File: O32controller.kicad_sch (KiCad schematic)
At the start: 39 parts, among them J1 SWD Connector, J12 I2C/RS485_2, J2 BATT+, J3 BATT-, J7 BATT+, J8 BATT-, J9 I2C/RS485_1, U1 MA702GQ-P, U2 STSPIN32F0A

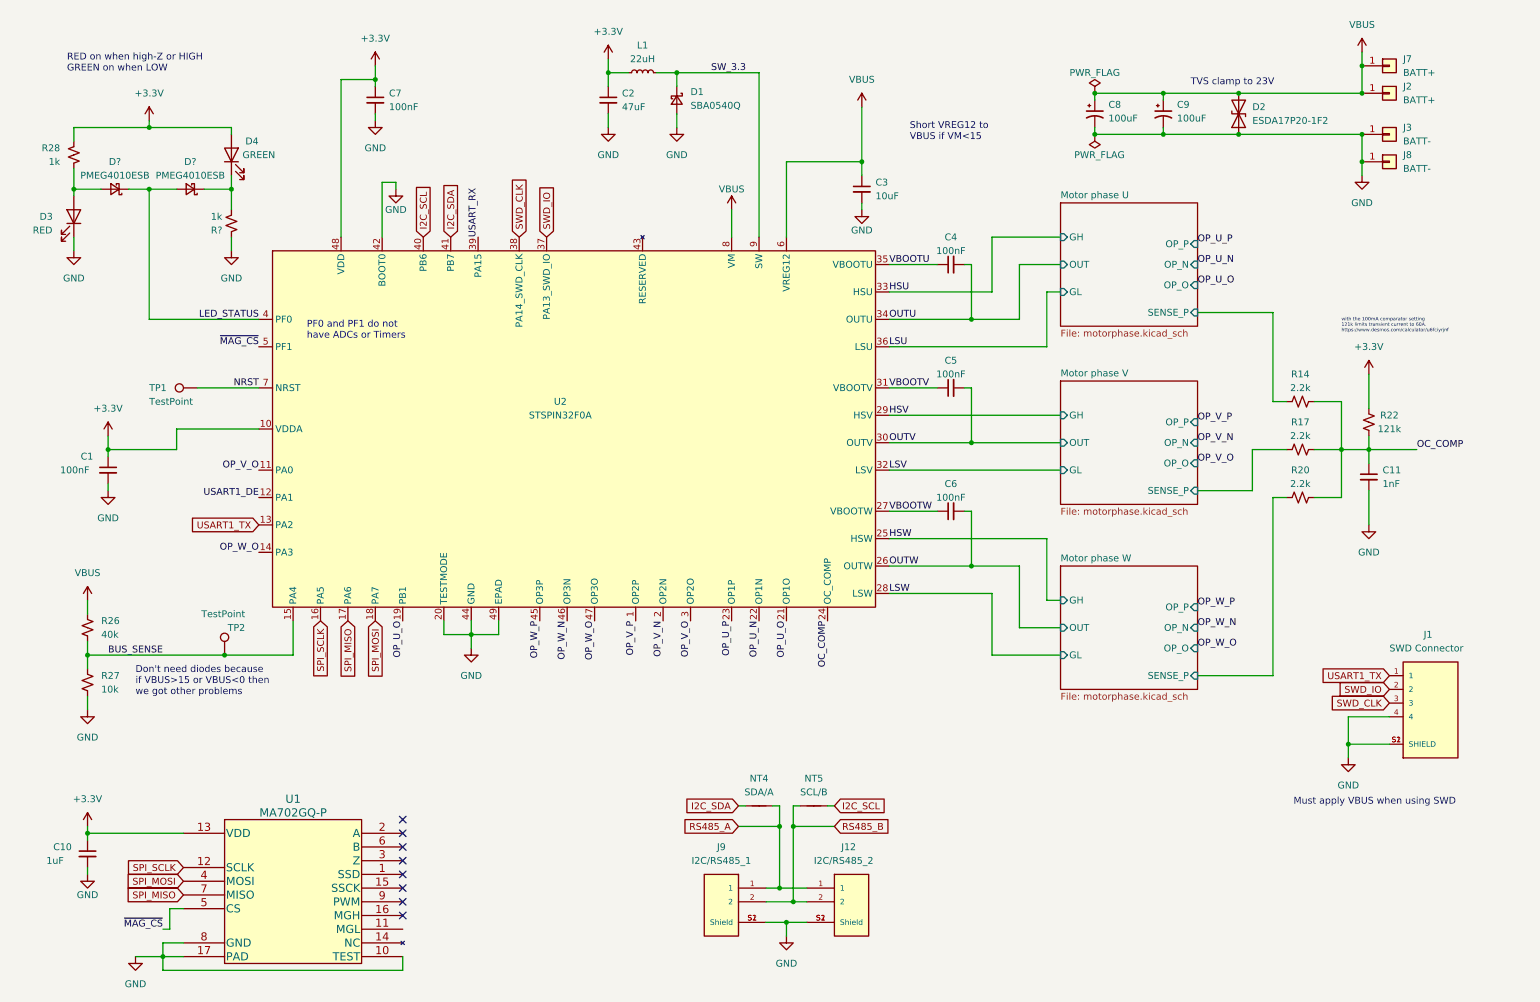
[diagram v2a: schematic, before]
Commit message: added rs485 and placed ma702
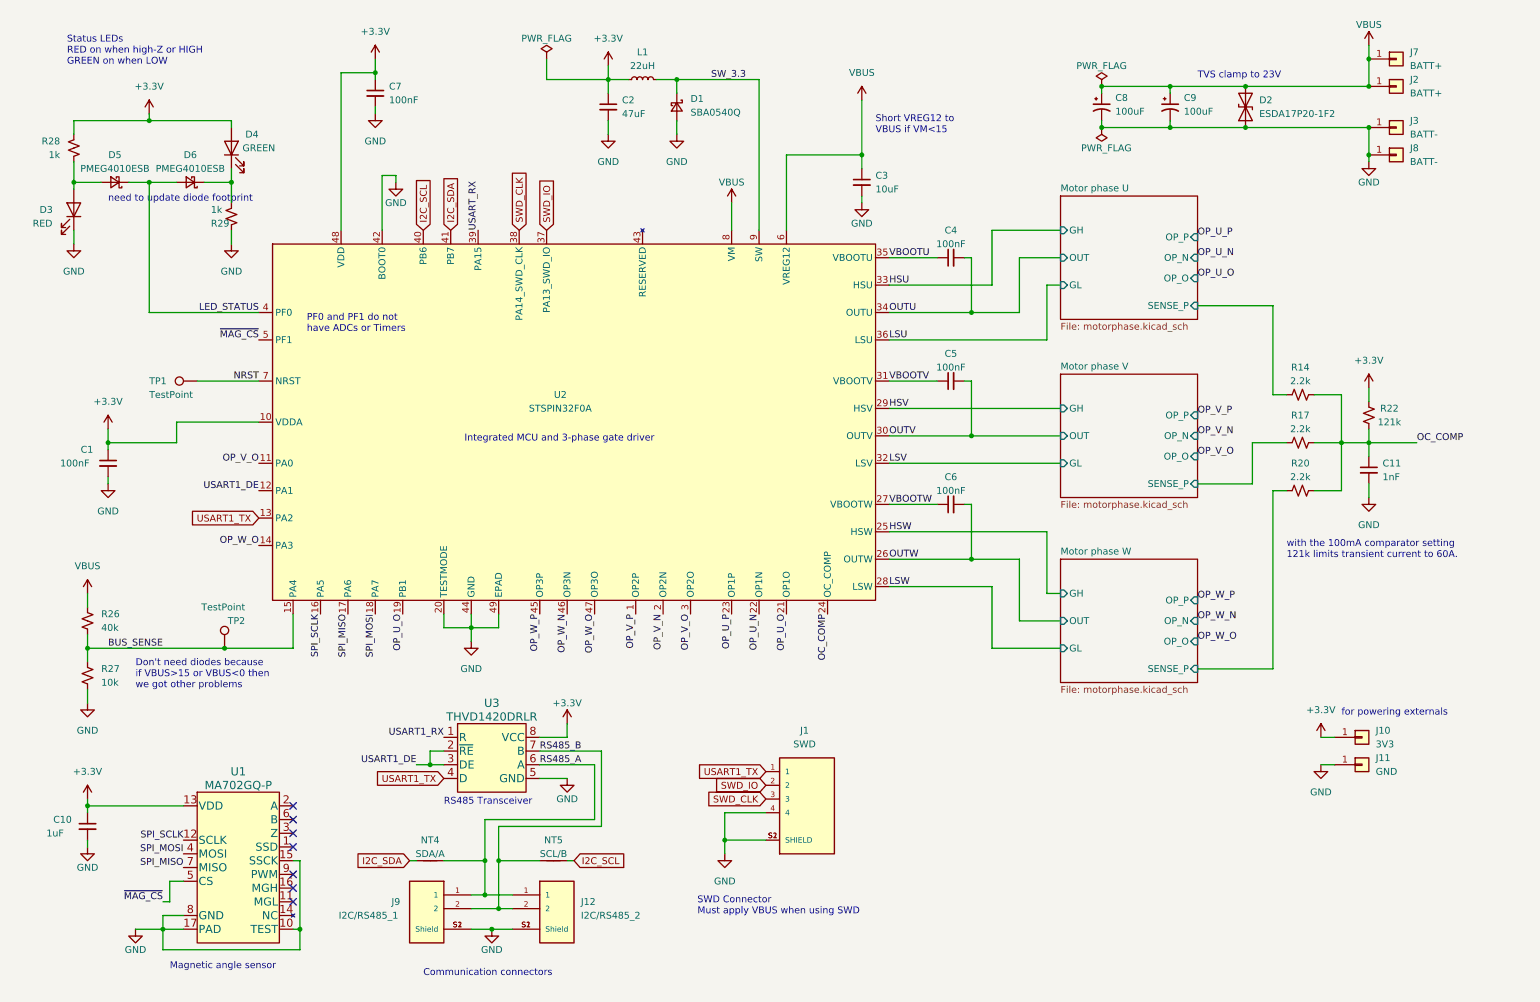
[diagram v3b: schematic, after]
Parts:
- added J10: 3V3, Connector_Wire:SolderWire-0.1sqmm_1x01_D0.4mm_OD1mm, symbol Connector_Generic:Conn_01x01
- added J11: GND, Connector_Wire:SolderWire-0.1sqmm_1x01_D0.4mm_OD1mm, symbol Connector_Generic:Conn_01x01
- added U3: THVD1420DRLR, O32controller:THVD1420DRLR_SOT-585, symbol O32controller:THVD1420DRLR
- D3, D4: footprint (none) -> LED_SMD:LED_0603_1608Metric
- D6: renamed from D?; footprint (none) -> O32controller:SDM2U30CSP-7
- J1: value SWD Connector -> SWD
- R26, R27, R28: footprint (none) -> Resistor_SMD:R_0402_1005Metric
- R29: renamed from R?; footprint (none) -> Resistor_SMD:R_0402_1005Metric
- TP1, TP2: footprint (none) -> TestPoint:TestPoint_Pad_D1.0mm
- gave numbers to parts that had none: 1
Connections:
- net +3.3V: now also J10.1 (Pin_1), U3.8 (VCC)
- net GND: now also U1.15 (SSCK), J11.1 (Pin_1), U3.5 (GND)
- net RS485_A: now also U3.6 (A)
- net RS485_B: now also U3.7 (B)
- net USART1_DE: now also U3.2 (~{RE}), U3.3 (DE)
- net USART1_TX: now also U3.4 (D)
- new net USART1_RX: U3.1 (R)
- no-connect marks 8 -> 7
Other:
- note added: "Communication connectors"
- note added: "Integrated MCU and 3-phase gate driver"
- note added: "Magnetic angle sensor"
- note added: "RS485 Transceiver"
- note added: "SWD Connector Must apply VBUS when using SWD"
- note added: "Status LEDs RED on when high-Z or HIGH GREEN on when LOW"
- note added: "for powering externals"
- note added: "need to update diode footprint"
- note added: "with the 100mA comparator setting 121k limits transient current to 60A."
- note removed: "Must apply VBUS when using SWD"
- note removed: "RED on when high-Z or HIGH GREEN on when LOW"
- note removed: "with the 100mA comparator setting 121k limits transient current to 60A. https://www.desmos.com/calculator/u6fciyrjnf"
- moved on the sheet: C1, C10, C11, C2, C3, C4, C5, C6, C7, C8, C9, D1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

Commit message: ahh my resistor schematic is old:
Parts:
- removed TP1: TestPoint, TestPoint:TestPoint_Pad_D1.0mm, symbol Connector:TestPoint
- added SW1: RESET, O32controller:Tactile_Switch_EVQ-P7A01P, symbol Switch:SW_Push
- D1: value SBA0540Q -> SDM2U30CSP; footprint Diode_SMD:D_DFN2L -> O32controller:SDM2U30CSP-7
- D5, D6: value PMEG4010ESB -> SDM2U30CSP
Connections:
- net GND: now also SW1.1
- net NRST: now also SW1.2
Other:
- note removed: "need to update diode footprint"
- moved on the sheet: C2, D1, L1

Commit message: woohoo everything connected, no drc err
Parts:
- C2: MP (none) -> GRM188R60J476ME15D
- C3: MP (none) -> GRM188R6YA106MA73D
- J10, J11: footprint Connector_Wire:SolderWire-0.1sqmm_1x01_D0.4mm_OD1mm -> O32controller:SolderWire-Actual_1x01_D1.25mm_OD_2.3mm
- U1: MP (none) -> MA702GQ-P
- U2: MP (none) -> STSPIN32F0A
- U3: MP (none) -> THVD1420DRLR
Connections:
- net USART1_RX is gone; now on net USART_RX: U3.1 (R)
- net Green_Cathode: now reaches D4.1 (K), D6.1 (K), R29.1
- net Red_Anode: now reaches D3.2 (A), D5.2 (A), R28.1
- net USART1_DE renamed USART_DE
- net USART1_TX renamed USART_TX
